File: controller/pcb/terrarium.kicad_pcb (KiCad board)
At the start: 4 copper layers, 90 x 90 mm, 81 parts, among them K1 G3MB-202P, K2 G3MB-202P, K3 G3MB-202P, P1 USB_C_Plug_USB2.0, Q1 S8050, Q2 S8050, Q3 S8050, Q4 S8050, Q5 BC817, Q6 BC817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

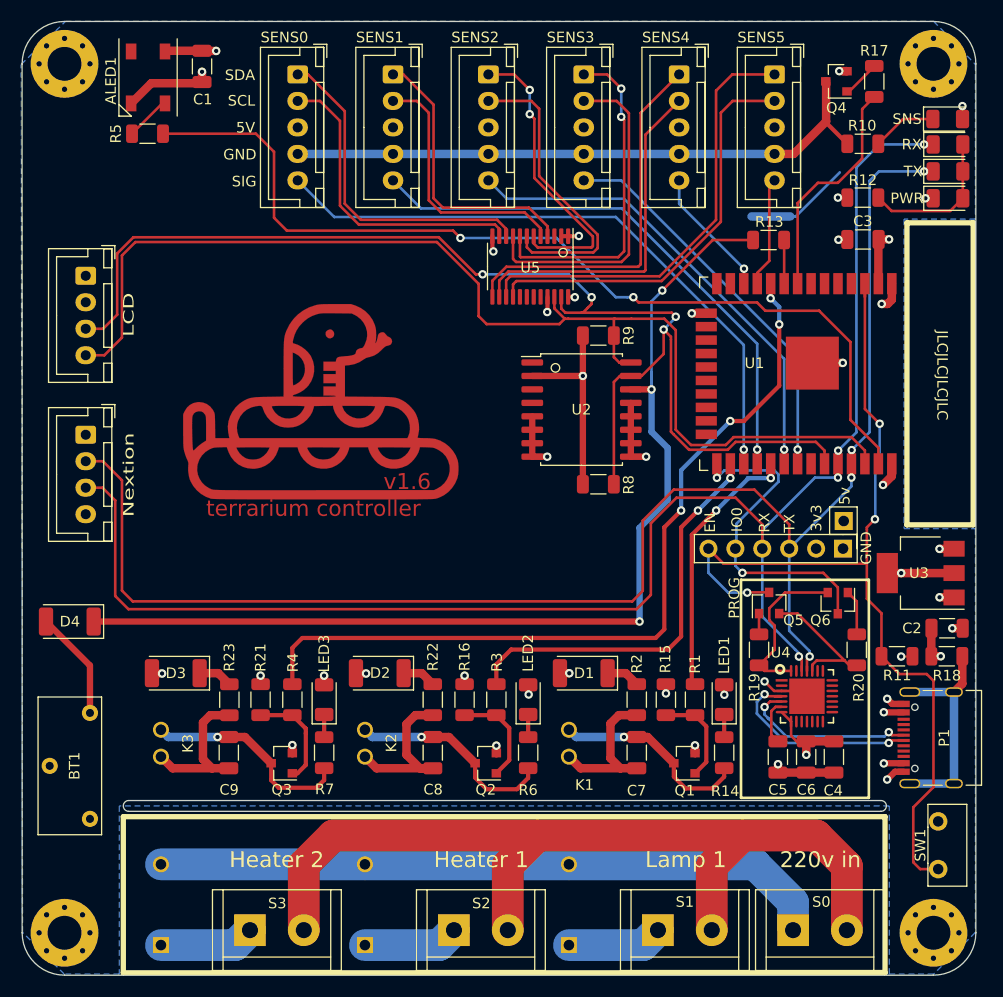
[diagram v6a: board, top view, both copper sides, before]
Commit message: Controller pcb/v1.7 (#5)
* move components around

* pcb v1.7 done

Co-authored-by: Grigorii Merkushev <brushknight@pop-os.localdomain>
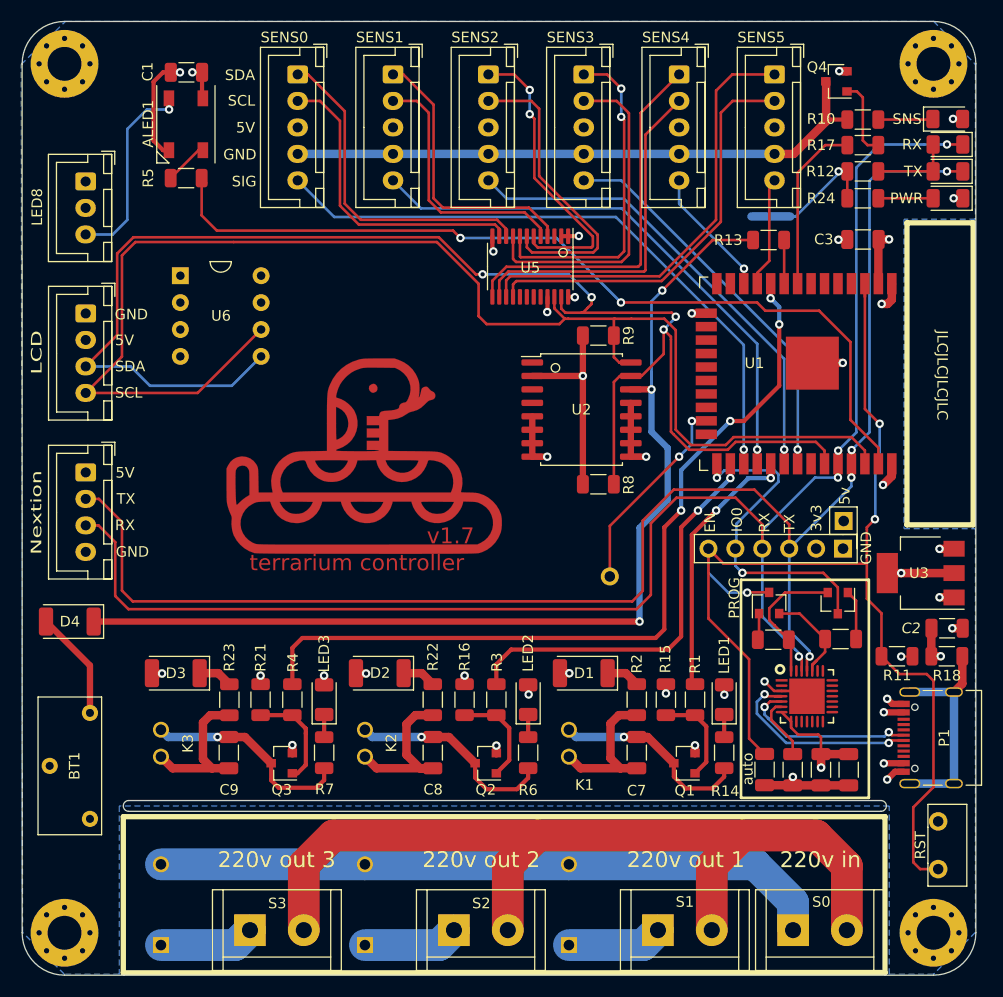
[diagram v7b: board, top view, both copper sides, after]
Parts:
- added C10: 0.47uF, Capacitor_SMD:C_1206_3216Metric, F.Cu at (111.1, 93.6)
- added LED8: LED, Connector_JST:JST_XH_B3B-XH-A_1x03_P2.50mm_Vertical, F.Cu at (47.0, 38.1)
- added R24: 5k, Resistor_SMD:R_1206_3216Metric, F.Cu at (120.3, 39.7)
- added RESET_EEPROM1: data, Connector_PinHeader_2.54mm:PinHeader_1x01_P2.54mm_Vertical, F.Cu at (96.5, 75.4)
- added U6: CAT24C256, Package_DIP:DIP-8_W7.62mm_Socket, F.Cu at (55.9, 47.0)
- Q5, Q6: value BC817 -> s8050
- R19, R20: value 10k -> 150
- R2, R22, R23: value 10 -> 470
- moved G*** 6.56 mm to (73.3, 64.0)
- moved R17 6.11 mm to (120.3, 34.7), turned to 0 degrees
- moved ALED1 5.68 mm to (56.5, 32.7)
- moved R5 5.55 mm to (56.5, 37.8)
- moved I2C1 3.56 mm to (47.0, 50.6)
- moved UART2 3.56 mm to (47.0, 65.6)
- moved R12 2.48 mm to (120.3, 37.1)
- moved R10 2.29 mm to (120.3, 32.3)
- moved C5 1.85 mm to (113.7, 93.6)
- moved C6 1.85 mm to (116.4, 93.6)
- moved C4 1.85 mm to (119.0, 93.6)
- moved R20 1.83 mm to (118.2, 81.3), turned to 0 degrees
- moved R19 1.65 mm to (111.9, 81.3), turned to 180 degrees
- moved C1 1.58 mm to (56.5, 27.8), turned to 180 degrees
- turned LED4 to 180 degrees
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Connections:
- net Net-(U1-Pad16) renamed G13
- LED6 pad 2: Net-(LED4-Pad2) -> Net-(LED6-Pad2)
- LED7 pad 2: Net-(LED4-Pad2) -> Net-(LED6-Pad2)
- R12 pad 2: Net-(LED4-Pad2) -> Net-(LED6-Pad2)
- U1 pad 23: Net-(U1-Pad23) -> G2
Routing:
- net EN: track 88.8 -> 110.4 mm
- net SCL: track 108.2 -> 129.7 mm
- net SDA: track 117.6 -> 138.6 mm
- net G2: track 0.00 -> 19.2 mm, vias 0 -> 2
- net Net-(ALED1-Pad2): track 0.00 -> 18.8 mm, vias 0 -> 1
- net Net-(LED4-Pad2): track 14.1 -> 5.17 mm
- net Net-(LED6-Pad2): track 0.00 -> 7.71 mm
- net G23: track 89.2 -> 83.0 mm
- net G32: track 21.7 -> 16.2 mm
- net GND: track 63.1 -> 67.6 mm
- net Net-(Q4-Pad1): track 3.51 -> 7.63 mm
- net Net-(Q5-Pad2): track 12.4 -> 9.40 mm
- net Net-(Q6-Pad2): track 15.6 -> 12.9 mm
- net +3V3: track 43.2 -> 45.7 mm
- net Net-(C5-Pad1): track 4.78 -> 6.04 mm
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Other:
- board text added: "220v out 1"
- board text added: "220v out 2"
- board text added: "220v out 3"
- board text added: "auto"
- board text added: "terrarium controller v1.7 github.com/brushknight/terrarium github.com/brushknight/terrarium-hardware"
- board text added: "v1.7"
- board text removed: "Heater 1"
- board text removed: "Heater 2"
- board text removed: "Lamp 1"
- board text removed: "terrarium controller v1.6 github.com/brushknight/terrarium github.com/brushknight/terrarium-hardware"
- board text removed: "v1.6"
